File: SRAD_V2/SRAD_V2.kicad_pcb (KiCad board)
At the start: 4 copper layers, 76.2 x 152.4 mm, 144 parts, among them IC1 STM32F767ZIT6, IC10 NCV81071BZR2G, IC2 LSM6DSVTR, IC3 MAX-M10S, IC4 MMC5983MA, IC5 AS5F31G04SND-08LIN, IC6 MS5607-02BA, IC7 TPS563200, IC8 TMCS1108A2UQDR, IC9 NCV81071BZR2G, J1 Conn_01x04_Pin, J2 S02B-XASS-1LFSN, J3 RSP-122811-02, J4 S02B-XASS-1LFSN, J5 Conn_01x02_Pin, M1 MountingHole_3.5mm_Pad, M2 MountingHole_3.5mm_Pad, M3 MountingHole_3.5mm_Pad, M4 MountingHole_3.5mm_Pad, Q1 NTMFS5C673NT1G, Q2 NTMFS5C673NT1G, Q3 NTMFS5C673NT1G, Q4 NTMFS5C673NT1G, Q5 MMBT3904LT3G, SW1 SLW-913535-2A-SMT, SW2 TS18-5-15-SL-160-SMT-TR, X1 Crystal

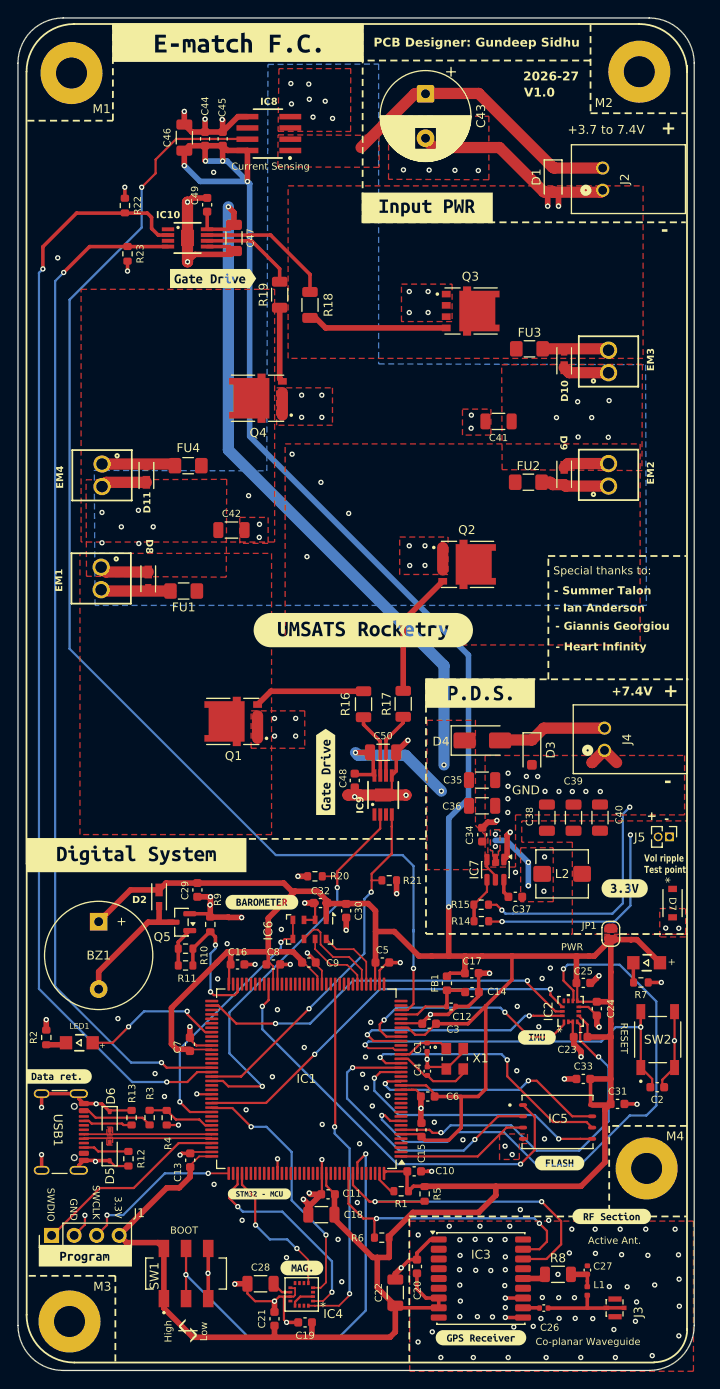
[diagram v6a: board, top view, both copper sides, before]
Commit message: Added External GPIO/ADC headers
Also impedance matched traces for USB and GPS input signal.
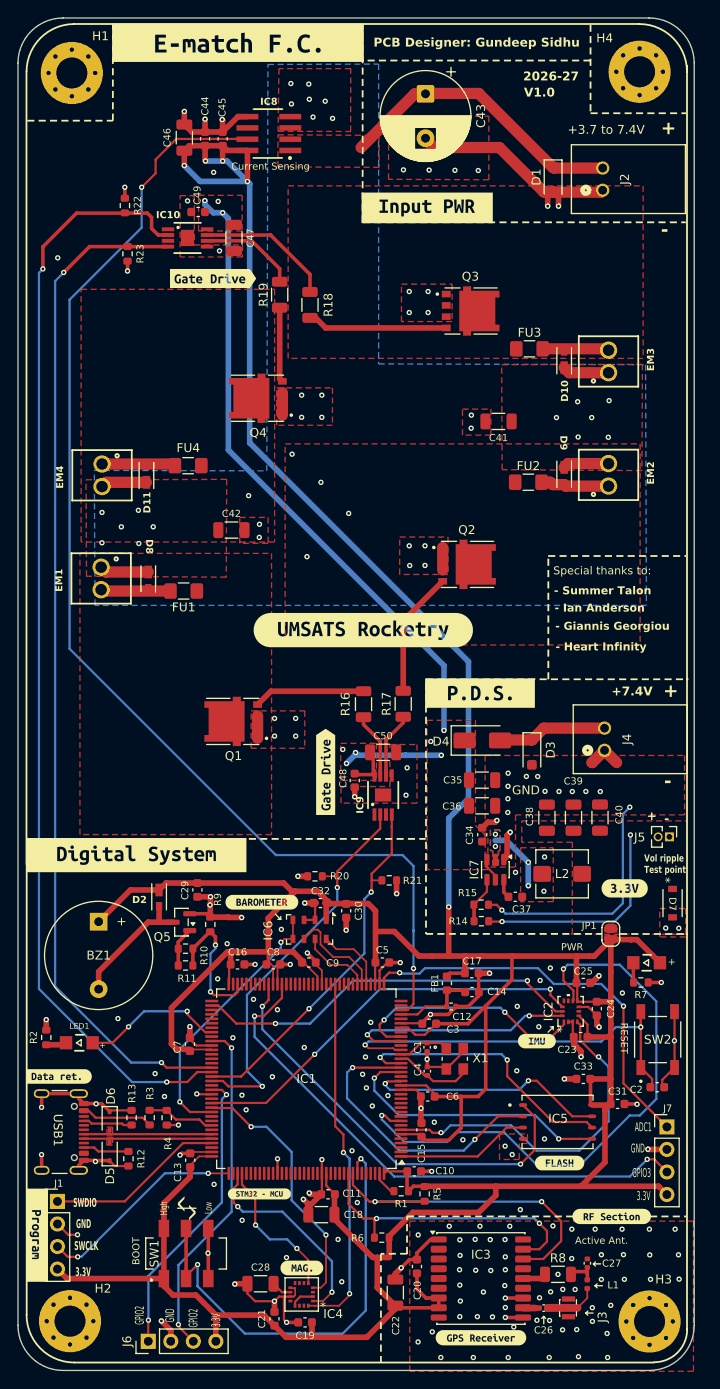
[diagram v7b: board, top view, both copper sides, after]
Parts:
- removed M1, M2, M3, M4: MountingHole_3.5mm_Pad, MountingHole:MountingHole_3.5mm_Pad
- added H1: MountingHole, MountingHole:MountingHole_3.5mm_Pad_Via, F.Cu at (62.3, 32.7)
- added H2: MountingHole, MountingHole:MountingHole_3.5mm_Pad_Via, F.Cu at (62.1, 173.4)
- added H3: MountingHole, MountingHole:MountingHole_3.5mm_Pad_Via, F.Cu at (127.4, 173.4)
- added H4: MountingHole, MountingHole:MountingHole_3.5mm_Pad_Via, F.Cu at (126.3, 32.6)
- added J6: Conn_01x04_Pin, Connector_PinHeader_2.54mm:PinHeader_1x04_P2.54mm_Vertical, F.Cu at (70.9, 175.7)
- added J7: Conn_01x04_Pin, Connector_PinHeader_2.54mm:PinHeader_1x04_P2.54mm_Vertical, F.Cu at (129.4, 151.5)
- moved kibuzzard-6A95C804 5.90 mm to (58.4, 163.7), turned to -90 degrees
- moved J3 5.25 mm to (118.3, 171.9)
- moved J1 3.88 mm to (60.7, 159.9), turned to 0 degrees
- moved SW1 2.26 mm to (75.2, 165.8)
- moved C49 1.30 mm to (76.6, 48.4), turned to 180 degrees
- moved L1 0.77 mm to (120.4, 169.2)
- moved C27 0.77 mm to (120.4, 166.9)
- moved kibuzzard-6A6394D1 0.41 mm to (114.7, 141.8)
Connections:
- C26 pad 2: Net-(C26-Pad2) -> /GPS_IN
- C41 pad 1: Net-(C41-Pad1) -> /E-match Firing Circuit/IN(-)
- IC8 pad 3: Net-(C41-Pad1) -> /E-match Firing Circuit/IN(-)
- J3 pad 1: Net-(C44-Pad2) -> /GPS_IN
- J3 pad 3: Net-(C44-Pad2) -> /GPS_IN
- L1 pad 2: Net-(C26-Pad2) -> /GPS_IN
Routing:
- net GPIO3: track 0.00 -> 62.2 mm, vias 0 -> 2
- net ADC1: track 0.00 -> 45.6 mm, vias 0 -> 2
- net GPIO1: track 0.00 -> 38.8 mm, vias 0 -> 2
- net GPIO2: track 0.00 -> 33.3 mm, vias 0 -> 2
- net GND: track 283.1 -> 256.3 mm, vias 209 -> 216
- net +3.3V: track 497.6 -> 511.6 mm
- net +7.4VBATT: track 101.1 -> 90.9 mm, vias 4 -> 6
- net Net-(C44-Pad2): track 10.1 -> 0.00 mm
- net /GPS_IN: track 0.00 -> 5.98 mm
- net SWCLK: track 18.4 -> 23.7 mm
- net SWDIO: track 22.4 -> 20.2 mm
- net EM_CH1: track 46.9 -> 45.2 mm
- net Net-(IC1-BOOT0): track 50.4 -> 51.6 mm
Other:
- board text added: "<--- 1 OZ COPPER"
- board text added: "ADC1"
- board text added: "FR4 7628 RC46% DK:4.74"
- board text added: "GPIO2"
- board text added: "GPIO3"
- board text removed: "<--- 0.5/1 OZ COPPER"
- board text removed: "Co-planar Waveguide"
- board text removed: "FR4 DK:4.74"

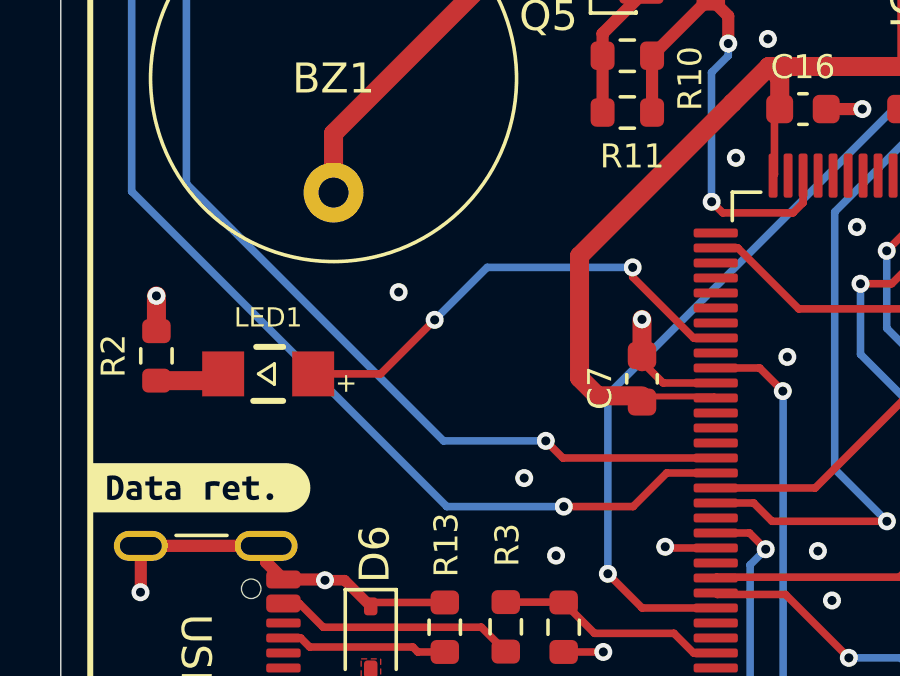
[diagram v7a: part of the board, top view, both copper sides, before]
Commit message: Added GPS Led
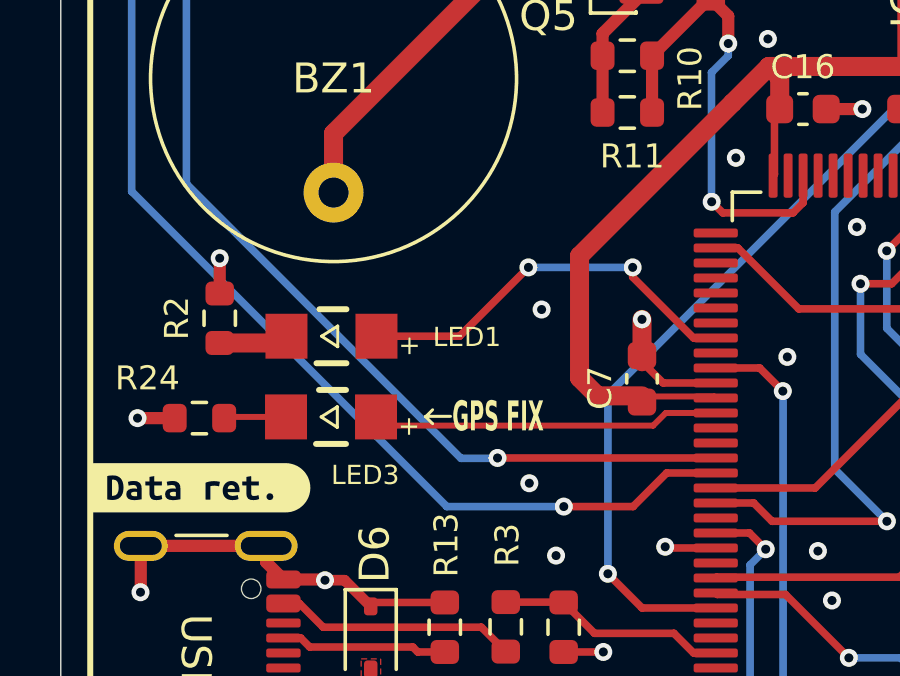
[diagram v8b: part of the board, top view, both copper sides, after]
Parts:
- added LED3: WL-SMCW_1206, 150120SS75000:WL-SMCW_1206, F.Cu at (65.3, 143.5)
- added R24: 806R, Resistor_SMD:R_0603_1608Metric, F.Cu at (60.9, 143.5)
- moved R2 2.46 mm to (61.6, 140.2)
- moved LED1 2.46 mm to (65.3, 140.8)
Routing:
- net GPS_FIX_LED: track 0.00 -> 11.6 mm
- net Net-(IC1-PD11): track 16.3 -> 13.8 mm
- net Net-(LED3-Pad1): track 0.00 -> 2.08 mm
- net GND: track 256.3 -> 257.6 mm, vias 216 -> 217
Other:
- board text added: "GPS FIX"
